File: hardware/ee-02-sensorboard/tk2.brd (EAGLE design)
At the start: 77.5 x 52.4 mm, 34 parts, among them J1 Debug, J2 AFE3_IDC_CABLE, J3 OPC_N3_CONNECTOR, U11 LM1117-5, U3 EE02, U4 ADS124S08, U5 CHIPCAP2SMD, U6 MAX14830, U7 ORIGIN GPS, U8 EE-NBIOT-01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

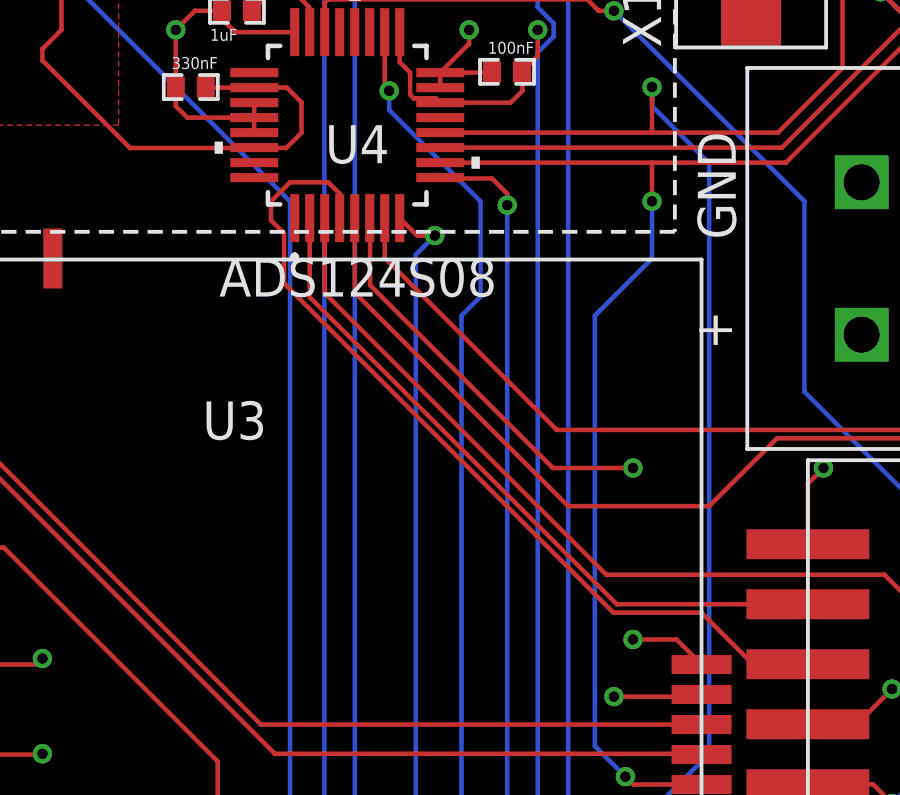
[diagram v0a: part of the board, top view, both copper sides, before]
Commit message: Updated schematics and layout. Fixed missing common signal on ADC.
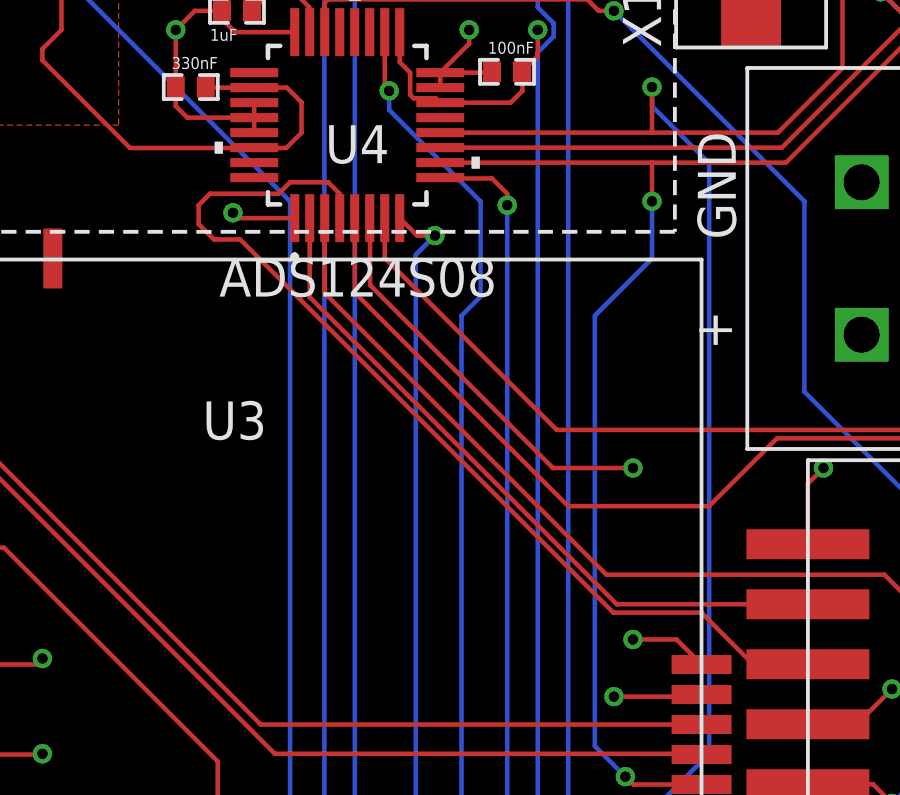
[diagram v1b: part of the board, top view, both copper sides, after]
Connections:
- net GND: now also U4.1, U8.GND@2, U8.GND@5
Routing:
- net N$15: track 29.2 -> 33.0 mm
- net GND: track 107.9 -> 110.0 mm, vias 42 -> 43
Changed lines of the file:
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@@
 <wire x1="55.6606" y1="32.0094" x2="55.805" y2="31.865" width="0.1524" layer="1"/>
 <wire x1="54.8017" y1="32.8683" x2="54.8017" y2="32.12843125" width="0.1524" layer="1"/>
+<contactref element="U4" pad="1"/>
+<wire x1="50.955" y1="28.015" x2="49.074" y2="28.015" width="0.1524" layer="1"/>
+<wire x1="49.074" y1="28.015" x2="48.895" y2="28.194" width="0.1524" layer="1"/>
+<via x="48.895" y="28.194" extent="1-16" drill="0.35"/>
+<contactref element="U8" pad="GND@5"/>
+<contactref element="U8" pad="GND@2"/>
 </signal>
 <signal name="+3V3">
@@
 <wire x1="52.451" y1="28.019" x2="52.451" y2="28.829" width="0.1524" layer="1"/>
 <wire x1="52.451" y1="28.829" x2="52.07" y2="29.21" width="0.1524" layer="1"/>
-<wire x1="52.07" y1="29.21" x2="50.8" y2="29.21" width="0.1524" layer="1"/>
-<wire x1="50.8" y1="29.21" x2="50.165" y2="28.575" width="0.1524" layer="1"/>
-<wire x1="50.165" y1="28.575" x2="50.165" y2="27.94" width="0.1524" layer="1"/>
-<wire x1="50.5994" y1="25.8404625" x2="61.5742625" y2="14.8656" width="0.1524" layer="1"/>
-<wire x1="50.165" y1="27.94" x2="50.5994" y2="27.5056" width="0.1524" layer="1"/>
-<wire x1="50.5994" y1="27.5056" x2="50.5994" y2="25.8404625" width="0.1524" layer="1"/>
-<wire x1="61.5742625" y1="14.8656" x2="64.5094" y2="14.8656" width="0.1524" layer="1"/>
+<wire x1="50.8" y1="29.21" x2="52.07" y2="29.21" width="0.1524" layer="1"/>
+<wire x1="64.5094" y1="14.8656" x2="61.5742625" y2="14.8656" width="0.1524" layer="1"/>
 <wire x1="66.23" y1="13.145" x2="68.06" y2="13.145" width="0.1524" layer="1"/>
 <wire x1="64.5094" y1="14.8656" x2="66.23" y2="13.145" width="0.1524" layer="1"/>
+<wire x1="49.1348625" y1="27.305" x2="48.26" y2="27.305" width="0.1524" layer="1"/>
+<wire x1="48.26" y1="27.305" x2="47.752" y2="27.813" width="0.1524" layer="1"/>
+<wire x1="47.752" y1="27.813" x2="47.752" y2="28.448" width="0.1524" layer="1"/>
+<wire x1="47.752" y1="28.448" x2="48.133" y2="28.829" width="0.1524" layer="1"/>
+<wire x1="48.133" y1="28.829" x2="50.419" y2="28.829" width="0.1524" layer="1"/>
+<wire x1="50.419" y1="28.829" x2="50.8" y2="29.21" width="0.1524" layer="1"/>
+<wire x1="61.5742625" y1="14.8656" x2="49.1348625" y2="27.305" width="0.1524" layer="1"/>
 </signal>
 <signal name="N$24">
